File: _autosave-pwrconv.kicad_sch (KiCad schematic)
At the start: 29 parts, among them J1 Power In, J2 Power Out, U1 TPS5430DDA, U2 TPS5430DDA, U3 TPS5430DDA

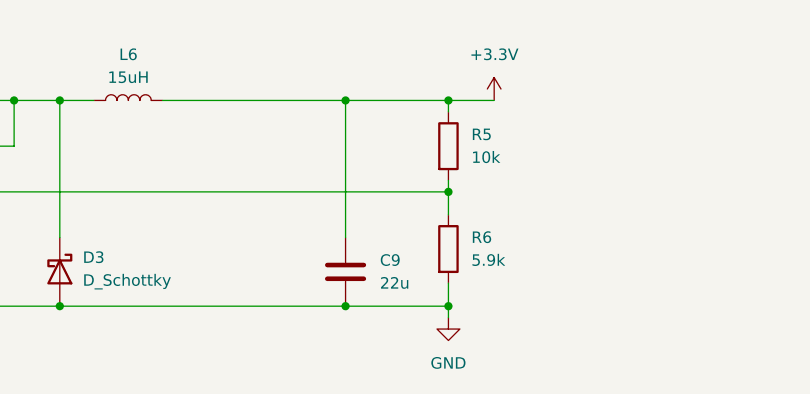
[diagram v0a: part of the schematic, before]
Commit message: added 3.3v converter
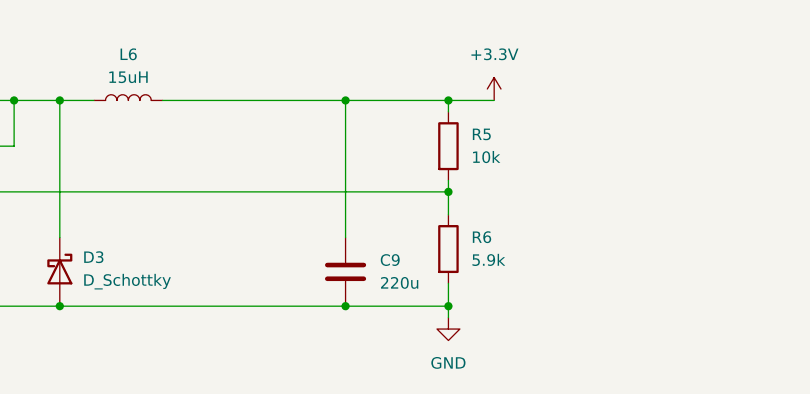
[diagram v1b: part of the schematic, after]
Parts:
- C9: value 22u -> 220u; LCSC C45783 -> C125977
- L6: LCSC C167223 -> C40000
- R6: LCSC C4410 -> C488883
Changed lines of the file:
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@@
 			)
 		)
-		(property "LCSC" "C167223"
+		(property "LCSC" "C40000"
 			(at 111.76 120.65 90)
 			(effects
@@
 			)
 		)
-		(property "LCSC" "C4410"
+		(property "LCSC" "C488883"
 			(at 147.32 137.16 0)
 			(effects
@@
 			)
 		)
-		(property "Value" "22u"
+		(property "Value" "220u"
 			(at 139.7 140.97 0)
 			(effects
@@
 			)
 		)
-		(property "LCSC" "C45783"
+		(property "LCSC" "C125977"
 			(at 135.89 139.7 0)
 			(effects
